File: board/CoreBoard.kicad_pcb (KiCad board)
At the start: 2 copper layers, 121.4 x 88.9 mm, 95 parts, among them J1 RJ45_LED_Shielded, J2 768250002, Q1 AO3401A, Q10 AO3401A, Q11 AO3401A, Q2 AO3401A, Q3 AO3401A, Q4 AO3401A, Q5 AO3401A, Q6 AO3401A, Q7 AO3401A, Q8 AO3401A, Q9 AO3401A, SW11 SW_Wuerth_450301014042, SW12 SW_Wuerth_450301014042, SW13 SW_Wuerth_450301014042, SW14 SW_Wuerth_450301014042, SW15 SW_Wuerth_450301014042, SW16 SW_Wuerth_450301014042, SW4 SW_Push, SW6 SW_Push, SW7 SW_Push, SW8 SW_Push, U1 74VHC138FT, U2 OKI-78SR-12_1.0-W36H-C, U3 SHHD003A0A, U4 GY-521, U5 Teensy4.1_DEV-16771, U6 MCP9808-E/MS

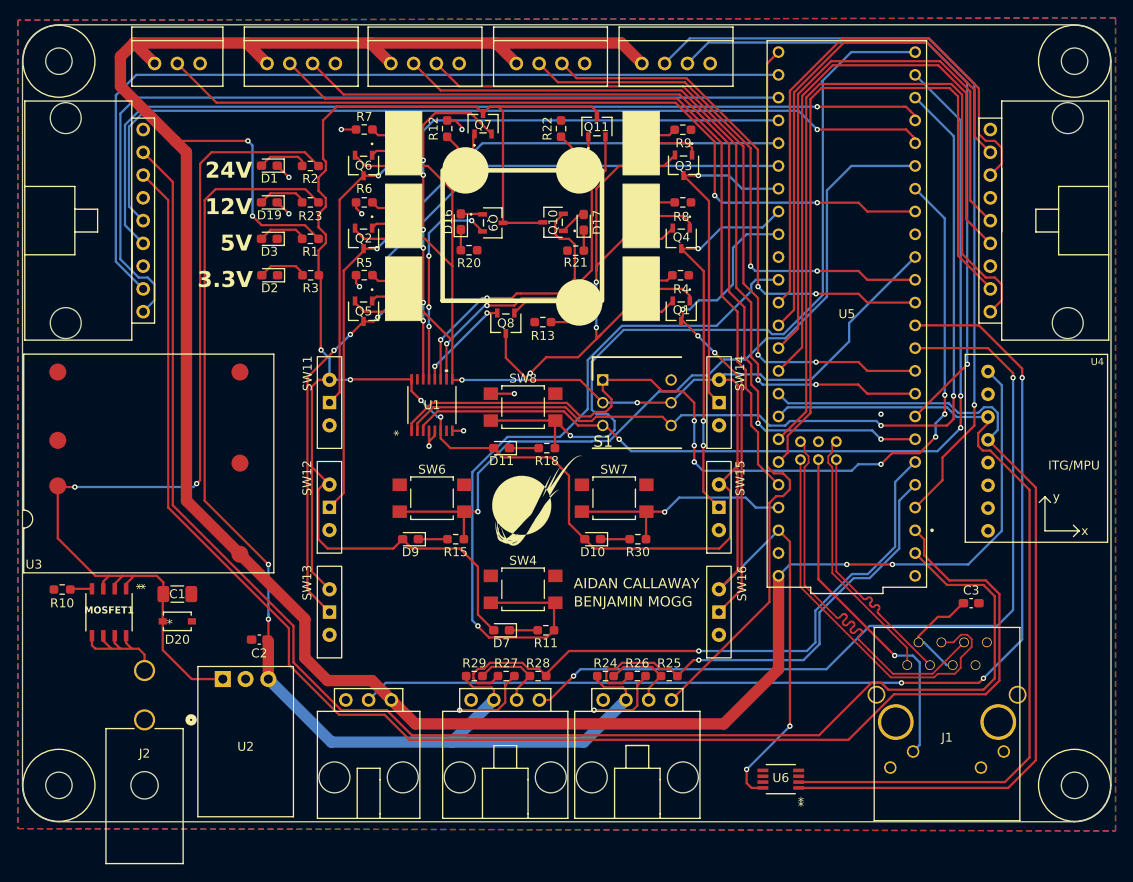
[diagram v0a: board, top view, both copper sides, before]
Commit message: Added Silkscreen and Pullup to both schematic and layout
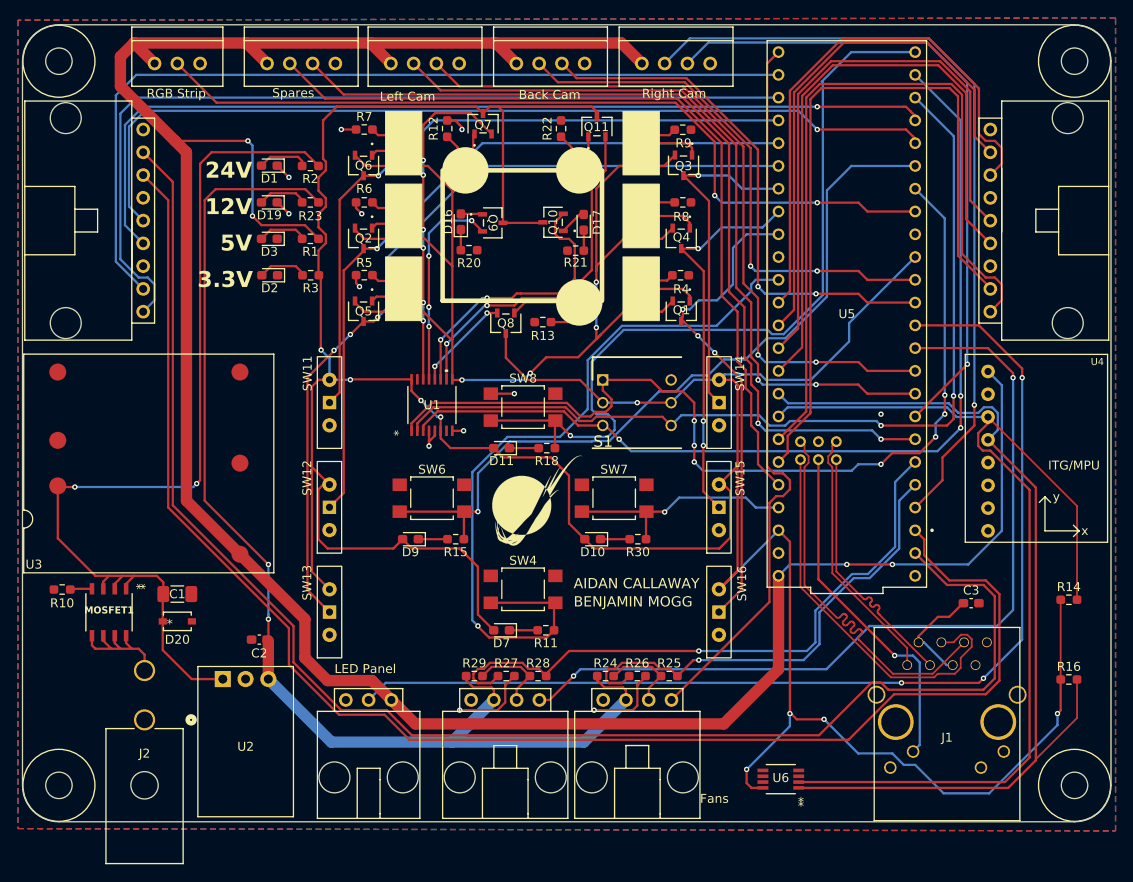
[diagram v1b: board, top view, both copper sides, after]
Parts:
- added R14: 4.7k, Resistor_SMD:R_0603_1608Metric_Pad0.98x0.95mm_HandSolder, F.Cu at (189.9, 114.9)
- added R16: 4.7k, Resistor_SMD:R_0603_1608Metric_Pad0.98x0.95mm_HandSolder, F.Cu at (189.9, 123.8)
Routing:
- net +3.3V: track 340.7 -> 391.5 mm, vias 7 -> 9
- net /Accelerometer/AccSCL: track 92.4 -> 116.9 mm
- net /Accelerometer/AccSDA: track 95.0 -> 105.8 mm
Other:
- board text added: "Back Cam"
- board text added: "Fans"
- board text added: "LED Panel"
- board text added: "Left Cam"
- board text added: "RGB Strip"
- board text added: "Right Cam"
- board text added: "Spares"

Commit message: Cleaned up traces and silkscreens
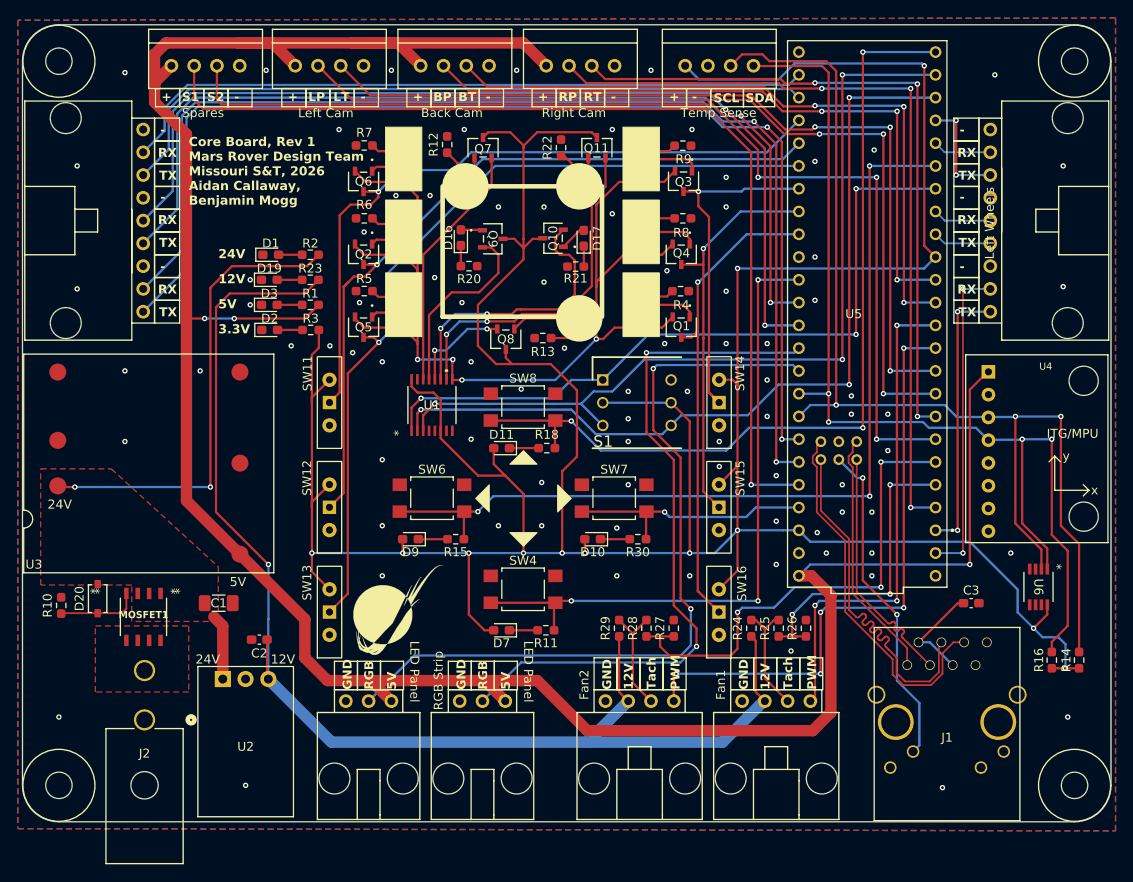
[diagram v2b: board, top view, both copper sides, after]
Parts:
- added Conn11: Molex_SL_04, MRDT_Connectors:MOLEX_SL_04_Vertical, F.Cu at (147.1, 55.4)
- Conn1: footprint MRDT_Connectors:MOLEX_SL_03_Vertical -> MRDT_Connectors:MOLEX_SL_03_Horizontal
- U6: footprint Temp_Sensor:MSOP8_MC_MCH-L -> CoreBoard:MSOP8_MC_MCH-L
- moved Conn1 81.2 mm to (127.0, 126.2), turned to 180 degrees
- moved U6 35.9 mm to (186.5, 113.5), turned to -90 degrees
- moved G*** 19.7 mm to (115.1, 116.1)
- moved R26 19.6 mm to (160.5, 118.1), turned to 90 degrees
- moved R27 19.4 mm to (145.8, 118.1), turned to 90 degrees
- moved R24 17.1 mm to (154.4, 118.1), turned to 90 degrees
- moved R29 17.0 mm to (139.7, 118.1), turned to 90 degrees
- moved Conn2 15.5 mm to (161.0, 126.2)
- moved Conn9 15.0 mm to (145.8, 126.2)
- moved R25 13.3 mm to (157.5, 118.1), turned to -90 degrees
- moved R28 13.2 mm to (142.7, 118.1), turned to -90 degrees
- moved Conn6 10.7 mm to (117.6, 55.4)
- moved Conn7 10.7 mm to (131.6, 55.4)
- moved Conn8 10.7 mm to (89.8, 55.4)
- moved Conn5 10.7 mm to (103.6, 55.4)
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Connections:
- D20 pad 2: GND -> Net-(MOSFET1-GATE)
- U5 pad 0: /Motor VESCs/FL_RX -> /Motor VESCs/BR_RX
- U5 pad 1: /Motor VESCs/FL_TX -> /Motor VESCs/BR_TX
- U5 pad 10: /Lighting/Lighting_Panel -> /Fans/PWM1
- U5 pad 14: /Motor VESCs/FR_TX -> /Motor VESCs/ML_TX
- U5 pad 15: /Motor VESCs/FR_RX -> /Motor VESCs/ML_RX
- U5 pad 16: /Motor VESCs/MR_RX -> /Lighting/RGB_Strip
- U5 pad 17: /Motor VESCs/MR_TX -> /Lighting/Lighting_Panel
- U5 pad 20: /Motor VESCs/BR_TX -> /Motor VESCs/BL_TX
- U5 pad 21: /Motor VESCs/BR_RX -> /Motor VESCs/BL_RX
- U5 pad 24: unconnected-(U5-A10-Pad24) -> /Motor VESCs/MR_TX
- U5 pad 25: /Lighting/RGB_Strip -> /Motor VESCs/MR_RX
- U5 pad 28: /Motor VESCs/ML_RX -> /Motor VESCs/FR_RX
- U5 pad 29: /Motor VESCs/ML_TX -> /Motor VESCs/FR_TX
- U5 pad 33: /Fans/PWM1 -> unconnected-(U5-MCLK2-Pad33)
- U5 pad 34: /Motor VESCs/BL_RX -> /Motor VESCs/FL_RX
- U5 pad 35: /Motor VESCs/BL_TX -> /Motor VESCs/FL_TX
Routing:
- net /Motor VESCs/FL_RX: track 168.7 -> 78.2 mm
- net /Motor VESCs/FL_TX: track 169.8 -> 80.1 mm
- net /Motor VESCs/MR_TX: track 70.6 -> 6.53 mm
- net /Motor VESCs/MR_RX: track 66.7 -> 6.53 mm
- net /Motor VESCs/BR_TX: track 85.0 -> 30.5 mm, vias 0 -> 2
- net /Motor VESCs/FR_RX: track 59.0 -> 6.53 mm
- net /Motor VESCs/FR_TX: track 61.8 -> 12.2 mm, vias 0 -> 2
- net /Motor VESCs/BR_RX: track 82.3 -> 35.6 mm, vias 0 -> 2
- net VCC: track 106.5 -> 60.2 mm
- net GND: track 35.2 -> 0.00 mm, vias 12 -> 87
- net /Lighting/Lighting_Panel: track 119.9 -> 87.8 mm, vias 3 -> 2
- net /Motor VESCs/BL_RX: track 97.7 -> 128.0 mm, vias 0 -> 2
- net /Motor VESCs/BL_TX: track 98.9 -> 127.2 mm, vias 0 -> 2
- net /Fans/PWM2: track 95.5 -> 68.1 mm, vias 2 -> 5
- net /Fans/PWM1: track 80.4 -> 55.3 mm, vias 0 -> 3
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- added copper zone on F.Cu, net Net-(J2-Pad2)
- added copper zone on F.Cu, net VCC
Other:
- board text added: "+"
- board text added: "-"
- board text added: "BP"
- board text added: "BT"
- board text added: "Core Board, Rev 1 Mars Rover Design Team Missouri S&T, 2026 Aidan Callaway, Benjamin Mogg"
- board text added: "Fan1"
- board text added: "Fan2"
- board text added: "GND"
- board text added: "LP"
- board text added: "LT"
- board text added: "Left Wheels"
- board text added: "PWM"
- board text added: "RGB"
- board text added: "RP"
- board text added: "RT"
- board text added: "RX"
- board text added: "S1"
- board text added: "S2"
- board text added: "SCL"
- board text added: "SDA"
- board text added: "TX"
- board text added: "Tach"
- board text added: "Temp Sense"
- board text removed: "AIDAN CALLAWAY"
- board text removed: "BENJAMIN MOGG"
- board text removed: "Fans"
